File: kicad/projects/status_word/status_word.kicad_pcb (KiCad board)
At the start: 2 copper layers, 203.2 x 97.8 mm, 9 parts, among them J1 peripheral_addr_bus_connector, J2 peripheral_aux_connector, J3 peripheral_membank_connector

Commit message: WIP on status word
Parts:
- added C2: C, Capacitor_THT:C_Disc_D5.0mm_W2.5mm_P5.00mm, F.Cu at (-15.6, 66.9)
- added C3: C, Capacitor_THT:C_Disc_D5.0mm_W2.5mm_P5.00mm, F.Cu at (-15.6, 71.0)
- added C4: C, Capacitor_THT:C_Disc_D5.0mm_W2.5mm_P5.00mm, F.Cu at (-15.6, 75.0)
- added C5: C, Capacitor_THT:C_Disc_D5.0mm_W2.5mm_P5.00mm, F.Cu at (-15.6, 79.1)
- added C6: C, Capacitor_THT:C_Disc_D5.0mm_W2.5mm_P5.00mm, F.Cu at (-15.6, 83.1)
- added C7: C, Capacitor_THT:C_Disc_D5.0mm_W2.5mm_P5.00mm, F.Cu at (-15.6, 87.2)
- added D1: LED, sixteen-bit-computer:LED_D5.0mm_Horizontal_O3.81mm_Z3.0mm, F.Cu at (251.5, 63.5)
- added D10: LED, sixteen-bit-computer:LED_D5.0mm_Horizontal_O3.81mm_Z3.0mm, F.Cu at (194.3, 63.5)
- added D11: LED, sixteen-bit-computer:LED_D5.0mm_Horizontal_O3.81mm_Z3.0mm, F.Cu at (188.0, 63.5)
- added D12: LED, sixteen-bit-computer:LED_D5.0mm_Horizontal_O3.81mm_Z3.0mm, F.Cu at (181.6, 63.5)
- added D13: LED, sixteen-bit-computer:LED_D5.0mm_Horizontal_O3.81mm_Z3.0mm, F.Cu at (175.3, 63.5)
- added D14: LED, sixteen-bit-computer:LED_D5.0mm_Horizontal_O3.81mm_Z3.0mm, F.Cu at (168.9, 63.5)
- added D15: LED, sixteen-bit-computer:LED_D5.0mm_Horizontal_O3.81mm_Z3.0mm, F.Cu at (162.6, 63.5)
- added D16: LED, sixteen-bit-computer:LED_D5.0mm_Horizontal_O3.81mm_Z3.0mm, F.Cu at (156.2, 63.5)
- added D2: LED, sixteen-bit-computer:LED_D5.0mm_Horizontal_O3.81mm_Z3.0mm, F.Cu at (245.1, 63.5)
- added D3: LED, sixteen-bit-computer:LED_D5.0mm_Horizontal_O3.81mm_Z3.0mm, F.Cu at (238.8, 63.5)
- added D4: LED, sixteen-bit-computer:LED_D5.0mm_Horizontal_O3.81mm_Z3.0mm, F.Cu at (232.4, 63.5)
- added D5: LED, sixteen-bit-computer:LED_D5.0mm_Horizontal_O3.81mm_Z3.0mm, F.Cu at (226.1, 63.5)
- added D6: LED, sixteen-bit-computer:LED_D5.0mm_Horizontal_O3.81mm_Z3.0mm, F.Cu at (219.7, 63.5)
- added D7: LED, sixteen-bit-computer:LED_D5.0mm_Horizontal_O3.81mm_Z3.0mm, F.Cu at (213.4, 63.5)
- added D8: LED, sixteen-bit-computer:LED_D5.0mm_Horizontal_O3.81mm_Z3.0mm, F.Cu at (207.0, 63.5)
- added D9: LED, sixteen-bit-computer:LED_D5.0mm_Horizontal_O3.81mm_Z3.0mm, F.Cu at (200.7, 63.5)
- added J10: Conn_01x02_Pin, Connector_PinHeader_2.54mm:PinHeader_1x02_P2.54mm_Vertical, F.Cu at (137.2, 53.3)
- added J11: Conn_01x02_Pin, Connector_PinHeader_2.54mm:PinHeader_1x02_P2.54mm_Vertical, F.Cu at (124.5, 53.3)
- added J12: Conn_01x02_Pin, Connector_PinHeader_2.54mm:PinHeader_1x02_P2.54mm_Vertical, F.Cu at (114.3, 53.3)
- added J13: Conn_01x02_Pin, Connector_PinHeader_2.54mm:PinHeader_1x02_P2.54mm_Vertical, F.Cu at (104.1, 53.3)
- added J14: Conn_01x08_Socket, Connector_PinSocket_2.54mm:PinSocket_1x08_P2.54mm_Horizontal, F.Cu at (61.0, 81.3)
- added J4: Conn_01x16_Socket, Connector_PinSocket_2.54mm:PinSocket_1x16_P2.54mm_Horizontal, F.Cu at (91.4, 61.0)
- added J5: Conn_01x04_Socket, Connector_PinSocket_2.54mm:PinSocket_1x04_P2.54mm_Horizontal, F.Cu at (61.0, 116.8)
- added J6: Conn_01x02_Pin, Connector_PinHeader_2.54mm:PinHeader_1x02_P2.54mm_Vertical, F.Cu at (109.2, 63.5)
- added J7: Conn_01x02_Pin, Connector_PinHeader_2.54mm:PinHeader_1x02_P2.54mm_Vertical, F.Cu at (119.4, 63.5)
- added J8: Conn_01x02_Pin, Connector_PinHeader_2.54mm:PinHeader_1x02_P2.54mm_Vertical, F.Cu at (132.1, 63.5)
- added J9: Conn_01x02_Pin, Connector_PinHeader_2.54mm:PinHeader_1x02_P2.54mm_Vertical, F.Cu at (144.8, 63.5)
- added RN1: R_Network08_US, Resistor_THT:R_Array_SIP9, F.Cu at (221.0, 71.1)
- added RN2: R_Network08_US, Resistor_THT:R_Array_SIP9, F.Cu at (170.2, 71.1)
- added RN3: R_Network08_US, Resistor_THT:R_Array_SIP9, F.Cu at (66.0, 101.6)
- added U1: 74HC10, Package_DIP:DIP-14_W7.62mm_Socket, F.Cu at (127.0, 132.1)
- added U2: 74HC377, Package_DIP:DIP-20_W7.62mm_Socket, F.Cu at (221.0, 132.1)
- added U3: 74HC377, Package_DIP:DIP-20_W7.62mm_Socket, F.Cu at (185.4, 132.1)
- added U4: 74HC245, Package_DIP:DIP-20_W7.62mm_Socket, F.Cu at (221.0, 114.3)
- added U5: 74HC245, Package_DIP:DIP-20_W7.62mm_Socket, F.Cu at (185.4, 114.3)
- added U6: 74HC245, Package_DIP:DIP-20_W7.62mm_Socket, F.Cu at (218.4, 86.4)
- added U7: 74HC245, Package_DIP:DIP-20_W7.62mm_Socket, F.Cu at (167.6, 86.4)
- moved C98 32.4 mm to (266.7, 83.8)
- moved C99 28.4 mm to (86.4, 124.5)
- moved C97 18.3 mm to (73.7, 71.1)
- turned J2 to 0 degrees
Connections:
- net /RFM renamed /MEM_ACT
- net /WTM renamed /~{RFM}/WTM

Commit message: Status word schematic complete - WIP on PCB.
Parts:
- removed TP1: TestPoint, Connector_Pin:Pin_D1.0mm_L10.0mm
- added J15: Conn_01x03_Pin, Connector_PinHeader_2.54mm:PinHeader_1x03_P2.54mm_Horizontal, F.Cu at (63.5, 111.8)
- added R1: 10K, Resistor_THT:R_Axial_DIN0207_L6.3mm_D2.5mm_P10.16mm_Horizontal, F.Cu at (27.9, 94.5)
- added R2: 10K, Resistor_THT:R_Axial_DIN0207_L6.3mm_D2.5mm_P10.16mm_Horizontal, F.Cu at (27.9, 98.6)
- added R3: 10K, Resistor_THT:R_Axial_DIN0207_L6.3mm_D2.5mm_P10.16mm_Horizontal, F.Cu at (27.9, 102.6)
- added R4: 10K, Resistor_THT:R_Axial_DIN0207_L6.3mm_D2.5mm_P10.16mm_Horizontal, F.Cu at (27.9, 106.7)
- RN1, RN2: value R_Network08_US -> 2K
- moved C3 235.1 mm to (213.4, 124.4), turned to 90 degrees
- moved C7 223.9 mm to (208.3, 86.3), turned to 90 degrees
- moved C4 202.0 mm to (180.3, 124.4), turned to 90 degrees
- moved C6 173.1 mm to (157.5, 86.3), turned to 90 degrees
- moved C2 172.7 mm to (147.3, 124.4), turned to 90 degrees
- moved C5 137.5 mm to (114.3, 124.4), turned to 90 degrees
- moved RN2 71.1 mm to (241.3, 72.4), turned to 180 degrees
- moved U2 68.8 mm to (152.4, 127.0)
- moved U5 67.3 mm to (119.4, 127.0)
- moved U6 55.9 mm to (162.6, 88.9)
- moved C97 51.1 mm to (22.6, 71.6)
- moved U1 48.3 mm to (124.5, 83.8)
- moved U7 45.8 mm to (213.4, 88.9)
- moved C1 38.8 mm to (119.4, 76.2), turned to -90 degrees
- moved U4 37.8 mm to (185.4, 127.0)
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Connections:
- C1 pad 1: unconnected-(C1-Pad1) -> VCC
- C1 pad 2: unconnected-(C1-Pad2) -> GND
- C2 pad 1: unconnected-(C2-Pad1) -> GND
- C2 pad 2: unconnected-(C2-Pad2) -> VCC
- C3 pad 1: unconnected-(C3-Pad1) -> GND
- C3 pad 2: unconnected-(C3-Pad2) -> VCC
- C4 pad 1: unconnected-(C4-Pad1) -> GND
- C4 pad 2: unconnected-(C4-Pad2) -> VCC
- C5 pad 1: unconnected-(C5-Pad1) -> GND
- C5 pad 2: unconnected-(C5-Pad2) -> VCC
- C6 pad 1: unconnected-(C6-Pad1) -> GND
- C6 pad 2: unconnected-(C6-Pad2) -> VCC
- C7 pad 1: unconnected-(C7-Pad1) -> GND
- C7 pad 2: unconnected-(C7-Pad2) -> VCC
- D1 pad 1: unconnected-(D1-K-Pad1) -> Net-(D1-K)
- D1 pad 2: unconnected-(D1-A-Pad2) -> Net-(D1-A)
- D10 pad 1: unconnected-(D10-K-Pad1) -> Net-(D10-K)
- D10 pad 2: unconnected-(D10-A-Pad2) -> Net-(D10-A)
- D11 pad 1: unconnected-(D11-K-Pad1) -> Net-(D11-K)
- D11 pad 2: unconnected-(D11-A-Pad2) -> Net-(D11-A)
- D12 pad 1: unconnected-(D12-K-Pad1) -> Net-(D12-K)
- D12 pad 2: unconnected-(D12-A-Pad2) -> Net-(D12-A)
- D13 pad 1: unconnected-(D13-K-Pad1) -> Net-(D13-K)
- D13 pad 2: unconnected-(D13-A-Pad2) -> Net-(D13-A)
- D14 pad 1: unconnected-(D14-K-Pad1) -> Net-(D14-K)
- D14 pad 2: unconnected-(D14-A-Pad2) -> Net-(D14-A)
- D15 pad 1: unconnected-(D15-K-Pad1) -> Net-(D15-K)
- D15 pad 2: unconnected-(D15-A-Pad2) -> Net-(D15-A)
- D16 pad 1: unconnected-(D16-K-Pad1) -> Net-(D16-K)
- D16 pad 2: unconnected-(D16-A-Pad2) -> Net-(D16-A)
- D2 pad 1: unconnected-(D2-K-Pad1) -> Net-(D2-K)
- D2 pad 2: unconnected-(D2-A-Pad2) -> Net-(D2-A)
- D3 pad 1: unconnected-(D3-K-Pad1) -> Net-(D3-K)
- D3 pad 2: unconnected-(D3-A-Pad2) -> Net-(D3-A)
- D4 pad 1: unconnected-(D4-K-Pad1) -> Net-(D4-K)
- D4 pad 2: unconnected-(D4-A-Pad2) -> Net-(D4-A)
- D5 pad 1: unconnected-(D5-K-Pad1) -> Net-(D5-K)
- D5 pad 2: unconnected-(D5-A-Pad2) -> Net-(D5-A)
- D6 pad 1: unconnected-(D6-K-Pad1) -> Net-(D6-K)
- D6 pad 2: unconnected-(D6-A-Pad2) -> Net-(D6-A)
- D7 pad 1: unconnected-(D7-K-Pad1) -> Net-(D7-K)
- D7 pad 2: unconnected-(D7-A-Pad2) -> Net-(D7-A)
- D8 pad 1: unconnected-(D8-K-Pad1) -> Net-(D8-K)
- D8 pad 2: unconnected-(D8-A-Pad2) -> Net-(D8-A)
- D9 pad 1: unconnected-(D9-K-Pad1) -> Net-(D9-K)
- D9 pad 2: unconnected-(D9-A-Pad2) -> Net-(D9-A)
- J1 pad 17: /ADDR_BUS_00 -> unconnected-(J1-A_00-Pad17)
- J1 pad 18: /ADDR_BUS_01 -> unconnected-(J1-A_01-Pad18)
- J1 pad 19: /ADDR_BUS_02 -> unconnected-(J1-A_02-Pad19)
- J1 pad 20: /ADDR_BUS_03 -> unconnected-(J1-A_03-Pad20)
- J1 pad 21: /ADDR_BUS_04 -> unconnected-(J1-A_04-Pad21)
- J1 pad 22: /ADDR_BUS_05 -> unconnected-(J1-A_05-Pad22)
- J1 pad 23: /ADDR_BUS_06 -> unconnected-(J1-A_06-Pad23)
- J1 pad 24: /ADDR_BUS_07 -> unconnected-(J1-A_07-Pad24)
- J1 pad 25: /ADDR_BUS_08 -> unconnected-(J1-A_08-Pad25)
- J1 pad 26: /ADDR_BUS_09 -> unconnected-(J1-A_09-Pad26)
- J1 pad 27: /ADDR_BUS_10 -> unconnected-(J1-A_10-Pad27)
- J1 pad 28: /ADDR_BUS_11 -> unconnected-(J1-A_11-Pad28)
- J1 pad 29: /ADDR_BUS_12 -> unconnected-(J1-A_12-Pad29)
- J1 pad 30: /ADDR_BUS_13 -> unconnected-(J1-A_13-Pad30)
- J1 pad 31: /ADDR_BUS_14 -> unconnected-(J1-A_14-Pad31)
- J1 pad 32: /ADDR_BUS_15 -> unconnected-(J1-A_15-Pad32)
- J10 pad 1: unconnected-(J10-Pin_1-Pad1) -> GND
- J10 pad 2: unconnected-(J10-Pin_2-Pad2) -> GND
- J11 pad 1: unconnected-(J11-Pin_1-Pad1) -> /CONTENT_14
- J11 pad 2: unconnected-(J11-Pin_2-Pad2) -> /CONTENT_14
- J12 pad 1: unconnected-(J12-Pin_1-Pad1) -> GND
- J12 pad 2: unconnected-(J12-Pin_2-Pad2) -> GND
- J13 pad 1: unconnected-(J13-Pin_1-Pad1) -> /CONTENT_15
- J13 pad 2: unconnected-(J13-Pin_2-Pad2) -> /CONTENT_15
- J14 pad 1: unconnected-(J14-Pin_1-Pad1) -> /EXT_7
- J14 pad 2: unconnected-(J14-Pin_2-Pad2) -> /EXT_6
- J14 pad 3: unconnected-(J14-Pin_3-Pad3) -> /EXT_5
- J14 pad 4: unconnected-(J14-Pin_4-Pad4) -> /EXT_4
- J14 pad 5: unconnected-(J14-Pin_5-Pad5) -> /EXT_3
- J14 pad 6: unconnected-(J14-Pin_6-Pad6) -> /EXT_2
- J14 pad 7: unconnected-(J14-Pin_7-Pad7) -> /EXT_1
- J14 pad 8: unconnected-(J14-Pin_8-Pad8) -> /EXT_0
- J2 pad 14: /RESET -> unconnected-(J2-RST-Pad14)
- J2 pad 8: /CTL_CLK -> unconnected-(J2-CCLK-Pad8)
- J3 pad 1: /BANK_BUS_00 -> unconnected-(J3-B_00-Pad1)
- J3 pad 10: /BANK_BUS_09 -> unconnected-(J3-B_09-Pad10)
- J3 pad 11: /BANK_BUS_10 -> unconnected-(J3-B_10-Pad11)
- J3 pad 12: /BANK_BUS_11 -> unconnected-(J3-B_11-Pad12)
- J3 pad 13: /BANK_BUS_12 -> unconnected-(J3-B_12-Pad13)
- J3 pad 14: /BANK_BUS_13 -> unconnected-(J3-B_13-Pad14)
- J3 pad 15: /BANK_BUS_14 -> unconnected-(J3-B_14-Pad15)
- J3 pad 16: /BANK_BUS_15 -> unconnected-(J3-B_15-Pad16)
- J3 pad 2: /BANK_BUS_01 -> unconnected-(J3-B_01-Pad2)
- J3 pad 3: /BANK_BUS_02 -> unconnected-(J3-B_02-Pad3)
- J3 pad 4: /BANK_BUS_03 -> unconnected-(J3-B_03-Pad4)
- J3 pad 5: /BANK_BUS_04 -> unconnected-(J3-B_04-Pad5)
- J3 pad 6: /BANK_BUS_05 -> unconnected-(J3-B_05-Pad6)
- J3 pad 7: /BANK_BUS_06 -> unconnected-(J3-B_06-Pad7)
- J3 pad 8: /BANK_BUS_07 -> unconnected-(J3-B_07-Pad8)
- J3 pad 9: /BANK_BUS_08 -> unconnected-(J3-B_08-Pad9)
- J4 pad 1: unconnected-(J4-Pin_1-Pad1) -> /CONTENT_00
- J4 pad 10: unconnected-(J4-Pin_10-Pad10) -> /CONTENT_09
- J4 pad 11: unconnected-(J4-Pin_11-Pad11) -> /CONTENT_10
- J4 pad 12: unconnected-(J4-Pin_12-Pad12) -> /CONTENT_11
- J4 pad 13: unconnected-(J4-Pin_13-Pad13) -> /CONTENT_12
- J4 pad 14: unconnected-(J4-Pin_14-Pad14) -> /CONTENT_13
- J4 pad 15: unconnected-(J4-Pin_15-Pad15) -> /CONTENT_14
- J4 pad 16: unconnected-(J4-Pin_16-Pad16) -> /CONTENT_15
- J4 pad 2: unconnected-(J4-Pin_2-Pad2) -> /CONTENT_01
- J4 pad 3: unconnected-(J4-Pin_3-Pad3) -> /CONTENT_02
- J4 pad 4: unconnected-(J4-Pin_4-Pad4) -> /CONTENT_03
- J4 pad 5: unconnected-(J4-Pin_5-Pad5) -> /CONTENT_04
- J4 pad 6: unconnected-(J4-Pin_6-Pad6) -> /CONTENT_05
- J4 pad 7: unconnected-(J4-Pin_7-Pad7) -> /CONTENT_06
- J4 pad 8: unconnected-(J4-Pin_8-Pad8) -> /CONTENT_07
- J4 pad 9: unconnected-(J4-Pin_9-Pad9) -> /CONTENT_08
- J5 pad 1: unconnected-(J5-Pin_1-Pad1) -> /ADDRESSED
- J5 pad 2: unconnected-(J5-Pin_2-Pad2) -> /ADDRESSED
- J5 pad 3: unconnected-(J5-Pin_3-Pad3) -> /ADDRESSED
- J5 pad 4: unconnected-(J5-Pin_4-Pad4) -> /ADDRESSED
- J6 pad 1: unconnected-(J6-Pin_1-Pad1) -> GND
- J6 pad 2: unconnected-(J6-Pin_2-Pad2) -> GND
- J7 pad 1: unconnected-(J7-Pin_1-Pad1) -> /CONTENT_12
- J7 pad 2: unconnected-(J7-Pin_2-Pad2) -> /CONTENT_12
- J8 pad 1: unconnected-(J8-Pin_1-Pad1) -> GND
- J8 pad 2: unconnected-(J8-Pin_2-Pad2) -> GND
- J9 pad 1: unconnected-(J9-Pin_1-Pad1) -> /CONTENT_13
- J9 pad 2: unconnected-(J9-Pin_2-Pad2) -> /CONTENT_13
- RN1 pad 1: unconnected-(RN1-common-Pad1) -> GND
- RN1 pad 2: unconnected-(RN1-R1-Pad2) -> Net-(D9-K)
- RN1 pad 3: unconnected-(RN1-R2-Pad3) -> Net-(D10-K)
- RN1 pad 4: unconnected-(RN1-R3-Pad4) -> Net-(D11-K)
- RN1 pad 5: unconnected-(RN1-R4-Pad5) -> Net-(D12-K)
- RN1 pad 6: unconnected-(RN1-R5-Pad6) -> Net-(D13-K)
- RN1 pad 7: unconnected-(RN1-R6-Pad7) -> Net-(D14-K)
- RN1 pad 8: unconnected-(RN1-R7-Pad8) -> Net-(D15-K)
- RN1 pad 9: unconnected-(RN1-R8-Pad9) -> Net-(D16-K)
- RN2 pad 1: unconnected-(RN2-common-Pad1) -> GND
- RN2 pad 2: unconnected-(RN2-R1-Pad2) -> Net-(D1-K)
- RN2 pad 3: unconnected-(RN2-R2-Pad3) -> Net-(D2-K)
- RN2 pad 4: unconnected-(RN2-R3-Pad4) -> Net-(D3-K)
- RN2 pad 5: unconnected-(RN2-R4-Pad5) -> Net-(D4-K)
- RN2 pad 6: unconnected-(RN2-R5-Pad6) -> Net-(D5-K)
- RN2 pad 7: unconnected-(RN2-R6-Pad7) -> Net-(D6-K)
- RN2 pad 8: unconnected-(RN2-R7-Pad8) -> Net-(D7-K)
- RN2 pad 9: unconnected-(RN2-R8-Pad9) -> Net-(D8-K)
- RN3 pad 1: unconnected-(RN3-common-Pad1) -> GND
- RN3 pad 2: unconnected-(RN3-R1-Pad2) -> /EXT_0
- RN3 pad 3: unconnected-(RN3-R2-Pad3) -> /EXT_1
- RN3 pad 4: unconnected-(RN3-R3-Pad4) -> /EXT_2
- RN3 pad 5: unconnected-(RN3-R4-Pad5) -> /EXT_3
- RN3 pad 6: unconnected-(RN3-R5-Pad6) -> /EXT_4
- RN3 pad 7: unconnected-(RN3-R6-Pad7) -> /EXT_5
- RN3 pad 8: unconnected-(RN3-R7-Pad8) -> /EXT_6
- RN3 pad 9: unconnected-(RN3-R8-Pad9) -> /EXT_7
- U1 pad 1: unconnected-(U1-Pad1) -> /MEM_ACT
- U1 pad 10: unconnected-(U1-Pad10) -> /~{RFM}/WTM
- U1 pad 11: unconnected-(U1-Pad11) -> /~{RFM}/WTM
- U1 pad 12: unconnected-(U1-Pad12) -> /~{WTM}
- U1 pad 13: unconnected-(U1-Pad13) -> /~{RFM}/WTM
- U1 pad 14: unconnected-(U1D-VCC-Pad14) -> VCC
- U1 pad 2: unconnected-(U1-Pad2) -> /ADDRESSED
- U1 pad 3: unconnected-(U1-Pad3) -> /MEM_ACT
- U1 pad 4: unconnected-(U1-Pad4) -> /ADDRESSED
- U1 pad 5: unconnected-(U1-Pad5) -> /RFM/~{WTM}
- U1 pad 6: unconnected-(U1-Pad6) -> /~{RFM}
- U1 pad 7: unconnected-(U1D-GND-Pad7) -> GND
- U1 pad 8: unconnected-(U1-Pad8) -> /RFM/~{WTM}
- U1 pad 9: unconnected-(U1-Pad9) -> /~{RFM}/WTM
- U2 pad 1: unconnected-(U2-~{E}-Pad1) -> /~{WTM}
- U2 pad 10: unconnected-(U2-GND-Pad10) -> GND
- U2 pad 11: unconnected-(U2-CP-Pad11) -> /DATA_CLK
- U2 pad 12: unconnected-(U2-Q4-Pad12) -> /CONTENT_12
- U2 pad 13: unconnected-(U2-D4-Pad13) -> /DATA_BUS_12
- U2 pad 14: unconnected-(U2-D5-Pad14) -> /DATA_BUS_13
- U2 pad 15: unconnected-(U2-Q5-Pad15) -> /CONTENT_13
- U2 pad 16: unconnected-(U2-Q6-Pad16) -> /CONTENT_14
- U2 pad 17: unconnected-(U2-D6-Pad17) -> /DATA_BUS_14
- U2 pad 18: unconnected-(U2-D7-Pad18) -> /DATA_BUS_15
- U2 pad 19: unconnected-(U2-Q7-Pad19) -> /CONTENT_15
- U2 pad 2: unconnected-(U2-Q0-Pad2) -> /CONTENT_08
- U2 pad 20: unconnected-(U2-VCC-Pad20) -> VCC
- U2 pad 3: unconnected-(U2-D0-Pad3) -> /DATA_BUS_08
- U2 pad 4: unconnected-(U2-D1-Pad4) -> /DATA_BUS_09
- U2 pad 5: unconnected-(U2-Q1-Pad5) -> /CONTENT_09
- U2 pad 6: unconnected-(U2-Q2-Pad6) -> /CONTENT_10
- U2 pad 7: unconnected-(U2-D2-Pad7) -> /DATA_BUS_10
- U2 pad 8: unconnected-(U2-D3-Pad8) -> /DATA_BUS_11
- U2 pad 9: unconnected-(U2-Q3-Pad9) -> /CONTENT_11
- U3 pad 1: unconnected-(U3-~{E}-Pad1) -> /~{WTM}
- U3 pad 10: unconnected-(U3-GND-Pad10) -> GND
- U3 pad 11: unconnected-(U3-CP-Pad11) -> /DATA_CLK
- U3 pad 12: unconnected-(U3-Q4-Pad12) -> /CONTENT_04
- U3 pad 13: unconnected-(U3-D4-Pad13) -> /DATA_BUS_04
- U3 pad 14: unconnected-(U3-D5-Pad14) -> /DATA_BUS_05
- U3 pad 15: unconnected-(U3-Q5-Pad15) -> /CONTENT_05
- U3 pad 16: unconnected-(U3-Q6-Pad16) -> /CONTENT_06
- U3 pad 17: unconnected-(U3-D6-Pad17) -> /DATA_BUS_06
- U3 pad 18: unconnected-(U3-D7-Pad18) -> /DATA_BUS_07
- U3 pad 19: unconnected-(U3-Q7-Pad19) -> /CONTENT_07
- U3 pad 2: unconnected-(U3-Q0-Pad2) -> /CONTENT_00
- U3 pad 20: unconnected-(U3-VCC-Pad20) -> VCC
- U3 pad 3: unconnected-(U3-D0-Pad3) -> /DATA_BUS_00
- U3 pad 4: unconnected-(U3-D1-Pad4) -> /DATA_BUS_01
- U3 pad 5: unconnected-(U3-Q1-Pad5) -> /CONTENT_01
- U3 pad 6: unconnected-(U3-Q2-Pad6) -> /CONTENT_02
- U3 pad 7: unconnected-(U3-D2-Pad7) -> /DATA_BUS_02
- U3 pad 8: unconnected-(U3-D3-Pad8) -> /DATA_BUS_03
- U3 pad 9: unconnected-(U3-Q3-Pad9) -> /CONTENT_03
- U4 pad 10: unconnected-(U4-GND-Pad10) -> GND
- U4 pad 11: unconnected-(U4-B8-Pad11) -> /CONTENT_04
- U4 pad 12: unconnected-(U4-B7-Pad12) -> /CONTENT_03
- U4 pad 13: unconnected-(U4-B6-Pad13) -> /CONTENT_05
- U4 pad 14: unconnected-(U4-B5-Pad14) -> /CONTENT_02
- U4 pad 15: unconnected-(U4-B4-Pad15) -> /CONTENT_06
- U4 pad 16: unconnected-(U4-B3-Pad16) -> /CONTENT_01
- U4 pad 17: unconnected-(U4-B2-Pad17) -> /CONTENT_07
- U4 pad 18: unconnected-(U4-B1-Pad18) -> /CONTENT_00
- U4 pad 19: unconnected-(U4-~{OE}-Pad19) -> /~{RFM}
- U4 pad 2: unconnected-(U4-A1-Pad2) -> /DATA_BUS_00
- U4 pad 20: unconnected-(U4-VCC-Pad20) -> VCC
- U4 pad 3: unconnected-(U4-A2-Pad3) -> /DATA_BUS_07
- U4 pad 4: unconnected-(U4-A3-Pad4) -> /DATA_BUS_01
- U4 pad 5: unconnected-(U4-A4-Pad5) -> /DATA_BUS_06
- U4 pad 6: unconnected-(U4-A5-Pad6) -> /DATA_BUS_02
- U4 pad 7: unconnected-(U4-A6-Pad7) -> /DATA_BUS_05
- U4 pad 8: unconnected-(U4-A7-Pad8) -> /DATA_BUS_03
- U4 pad 9: unconnected-(U4-A8-Pad9) -> /DATA_BUS_04
- U5 pad 10: unconnected-(U5-GND-Pad10) -> GND
- U5 pad 11: unconnected-(U5-B8-Pad11) -> /EXT_0
- U5 pad 12: unconnected-(U5-B7-Pad12) -> /EXT_1
- U5 pad 13: unconnected-(U5-B6-Pad13) -> /EXT_2
- U5 pad 14: unconnected-(U5-B5-Pad14) -> /EXT_3
- U5 pad 15: unconnected-(U5-B4-Pad15) -> /EXT_4
- U5 pad 16: unconnected-(U5-B3-Pad16) -> /EXT_5
- U5 pad 17: unconnected-(U5-B2-Pad17) -> /EXT_6
- U5 pad 18: unconnected-(U5-B1-Pad18) -> /EXT_7
- U5 pad 19: unconnected-(U5-~{OE}-Pad19) -> /~{RFM}
- U5 pad 2: unconnected-(U5-A1-Pad2) -> /DATA_BUS_08
- U5 pad 20: unconnected-(U5-VCC-Pad20) -> VCC
- U5 pad 3: unconnected-(U5-A2-Pad3) -> /DATA_BUS_09
- U5 pad 4: unconnected-(U5-A3-Pad4) -> /DATA_BUS_10
- U5 pad 5: unconnected-(U5-A4-Pad5) -> /DATA_BUS_11
- U5 pad 6: unconnected-(U5-A5-Pad6) -> /DATA_BUS_12
- U5 pad 7: unconnected-(U5-A6-Pad7) -> /DATA_BUS_13
- U5 pad 8: unconnected-(U5-A7-Pad8) -> /DATA_BUS_14
- U5 pad 9: unconnected-(U5-A8-Pad9) -> /DATA_BUS_15
- U6 pad 1: unconnected-(U6-DIR-Pad1) -> VCC
- U6 pad 10: unconnected-(U6-GND-Pad10) -> GND
- U6 pad 11: unconnected-(U6-B8-Pad11) -> Net-(D9-A)
- U6 pad 12: unconnected-(U6-B7-Pad12) -> Net-(D10-A)
- U6 pad 13: unconnected-(U6-B6-Pad13) -> Net-(D11-A)
- U6 pad 14: unconnected-(U6-B5-Pad14) -> Net-(D12-A)
- U6 pad 15: unconnected-(U6-B4-Pad15) -> Net-(D13-A)
- U6 pad 16: unconnected-(U6-B3-Pad16) -> Net-(D14-A)
- U6 pad 17: unconnected-(U6-B2-Pad17) -> Net-(D15-A)
- U6 pad 18: unconnected-(U6-B1-Pad18) -> Net-(D16-A)
- U6 pad 19: unconnected-(U6-~{OE}-Pad19) -> /LED_~{OE}
- U6 pad 2: unconnected-(U6-A1-Pad2) -> /CONTENT_15
- U6 pad 20: unconnected-(U6-VCC-Pad20) -> VCC
- U6 pad 3: unconnected-(U6-A2-Pad3) -> /CONTENT_14
- U6 pad 4: unconnected-(U6-A3-Pad4) -> /CONTENT_13
- U6 pad 5: unconnected-(U6-A4-Pad5) -> /CONTENT_12
- U6 pad 6: unconnected-(U6-A5-Pad6) -> /CONTENT_11
- U6 pad 7: unconnected-(U6-A6-Pad7) -> /CONTENT_10
- U6 pad 8: unconnected-(U6-A7-Pad8) -> /CONTENT_09
- U6 pad 9: unconnected-(U6-A8-Pad9) -> /CONTENT_08
- U7 pad 1: unconnected-(U7-DIR-Pad1) -> VCC
- U7 pad 10: unconnected-(U7-GND-Pad10) -> GND
- U7 pad 11: unconnected-(U7-B8-Pad11) -> Net-(D1-A)
- U7 pad 12: unconnected-(U7-B7-Pad12) -> Net-(D2-A)
- U7 pad 13: unconnected-(U7-B6-Pad13) -> Net-(D3-A)
- U7 pad 14: unconnected-(U7-B5-Pad14) -> Net-(D4-A)
- U7 pad 15: unconnected-(U7-B4-Pad15) -> Net-(D5-A)
- U7 pad 16: unconnected-(U7-B3-Pad16) -> Net-(D6-A)
- U7 pad 17: unconnected-(U7-B2-Pad17) -> Net-(D7-A)
- U7 pad 18: unconnected-(U7-B1-Pad18) -> Net-(D8-A)
- U7 pad 19: unconnected-(U7-~{OE}-Pad19) -> /LED_~{OE}
- U7 pad 2: unconnected-(U7-A1-Pad2) -> /CONTENT_07
- U7 pad 20: unconnected-(U7-VCC-Pad20) -> VCC
- U7 pad 3: unconnected-(U7-A2-Pad3) -> /CONTENT_06
- U7 pad 4: unconnected-(U7-A3-Pad4) -> /CONTENT_05
- U7 pad 5: unconnected-(U7-A4-Pad5) -> /CONTENT_04
- U7 pad 6: unconnected-(U7-A5-Pad6) -> /CONTENT_03
- U7 pad 7: unconnected-(U7-A6-Pad7) -> /CONTENT_02
- U7 pad 8: unconnected-(U7-A7-Pad8) -> /CONTENT_01
- U7 pad 9: unconnected-(U7-A8-Pad9) -> /CONTENT_00
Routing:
- net /CONTENT_03: track 0.00 -> 44.2 mm
- net /CONTENT_01: track 0.00 -> 44.2 mm
- net /CONTENT_02: track 0.00 -> 44.2 mm
- net /CONTENT_00: track 0.00 -> 44.2 mm
- net /CONTENT_08: track 0.00 -> 41.4 mm
- net /CONTENT_11: track 0.00 -> 41.2 mm
- net /CONTENT_09: track 0.00 -> 41.2 mm
- net /CONTENT_10: track 0.00 -> 41.2 mm
- net /CONTENT_07: track 0.00 -> 36.6 mm
- net /CONTENT_05: track 0.00 -> 36.6 mm
- net /CONTENT_06: track 0.00 -> 35.6 mm
- net /CONTENT_04: track 0.00 -> 34.8 mm
- net /CONTENT_15: track 0.00 -> 33.0 mm
- net /CONTENT_14: track 0.00 -> 33.0 mm
- net /CONTENT_13: track 0.00 -> 33.0 mm
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
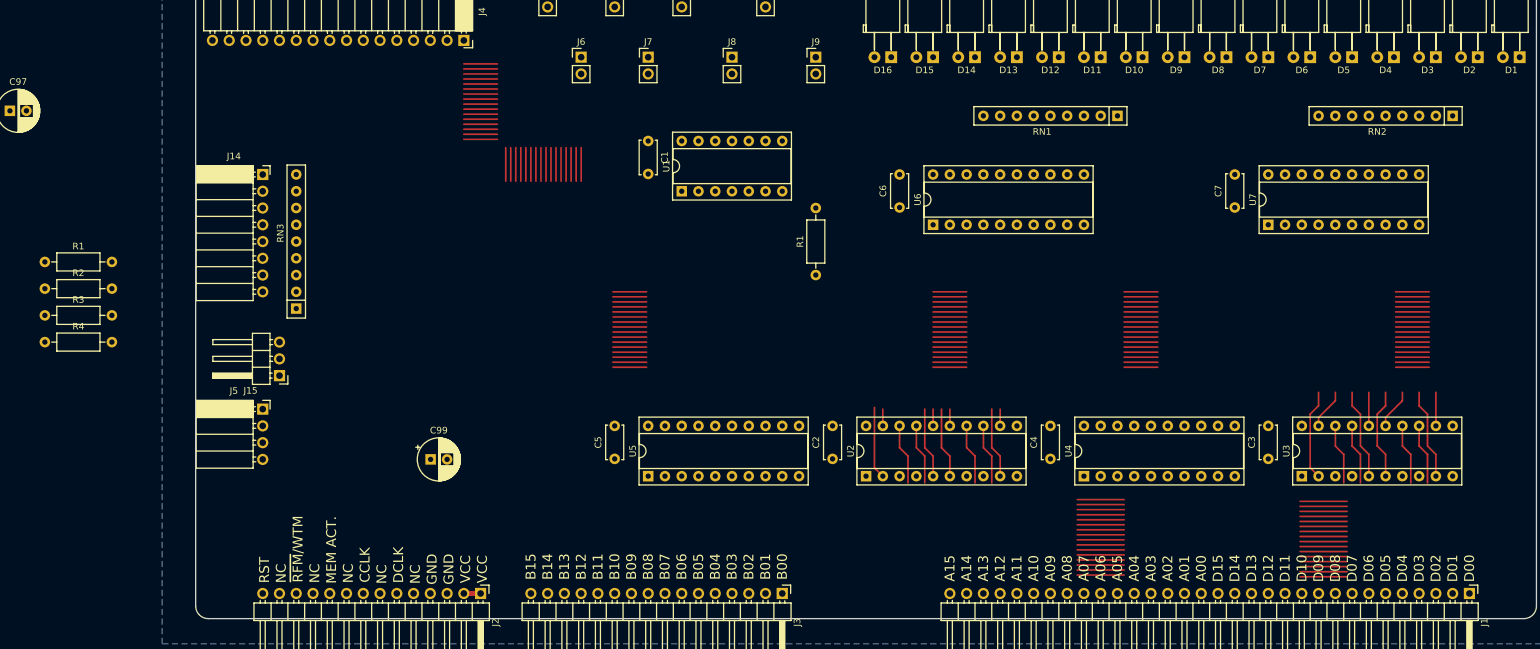
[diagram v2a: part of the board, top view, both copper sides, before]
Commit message: WIP on status word PCB
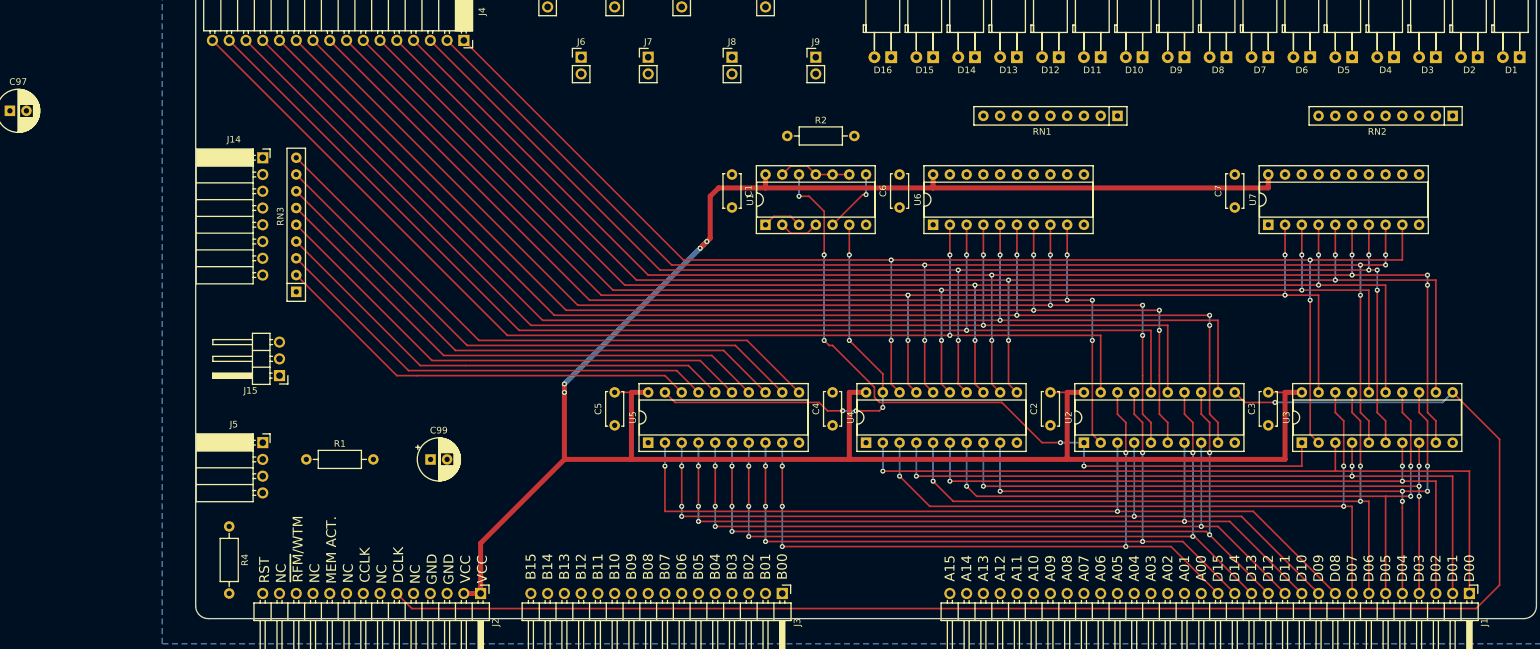
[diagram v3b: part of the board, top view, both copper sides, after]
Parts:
- removed the R1 at (144.8, 96.5)
- removed R3: 10K, Resistor_THT:R_Axial_DIN0207_L6.3mm_D2.5mm_P10.16mm_Horizontal
- moved R2 114.9 mm to (140.5, 75.4)
- moved R1 49.7 mm to (67.6, 124.5)
- moved R4 39.5 mm to (55.9, 134.6), turned to -90 degrees
- moved C2 33.4 mm to (180.3, 119.3)
- moved C4 33.4 mm to (147.3, 119.3)
- moved U2 33.4 mm to (185.4, 121.9)
- moved U4 33.4 mm to (152.4, 121.9)
- moved C1 13.7 mm to (132.1, 81.3)
- moved U1 13.7 mm to (137.2, 88.9)
- moved C3 5.08 mm to (213.4, 119.3)
- moved C5 5.08 mm to (114.3, 119.3)
- moved J5 5.08 mm to (61.0, 121.9)
- moved U3 5.08 mm to (218.4, 121.9)
- moved U5 5.08 mm to (119.4, 121.9)
- moved J14 2.54 mm to (61.0, 78.7)
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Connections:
- U5 pad 11: /EXT_0 -> /EXT_7
- U5 pad 12: /EXT_1 -> /EXT_6
- U5 pad 13: /EXT_2 -> /EXT_5
- U5 pad 14: /EXT_3 -> /EXT_4
- U5 pad 15: /EXT_4 -> /EXT_3
- U5 pad 16: /EXT_5 -> /EXT_2
- U5 pad 17: /EXT_6 -> /EXT_1
- U5 pad 18: /EXT_7 -> /EXT_0
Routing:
- net VCC: track 2.54 -> 337.5 mm, vias 0 -> 4
- net /DATA_CLK: track 0.00 -> 236.0 mm, vias 0 -> 1
- net /CONTENT_04: track 34.8 -> 214.7 mm, vias 0 -> 4
- net /CONTENT_03: track 44.2 -> 220.3 mm, vias 0 -> 6
- net /CONTENT_06: track 35.6 -> 209.5 mm, vias 0 -> 4
- net /CONTENT_05: track 36.6 -> 209.9 mm, vias 0 -> 4
- net /CONTENT_07: track 36.6 -> 204.0 mm, vias 0 -> 4
- net /CONTENT_02: track 44.2 -> 210.5 mm, vias 0 -> 6
- net /CONTENT_00: track 44.2 -> 210.2 mm, vias 0 -> 4
- net /CONTENT_01: track 44.2 -> 209.7 mm, vias 0 -> 6
- net /CONTENT_12: track 33.0 -> 187.8 mm, vias 0 -> 2
- net /CONTENT_11: track 41.2 -> 191.8 mm, vias 0 -> 4
- net /CONTENT_14: track 33.0 -> 183.3 mm, vias 0 -> 2
- net /CONTENT_13: track 33.0 -> 183.0 mm, vias 0 -> 2
- net /CONTENT_15: track 33.0 -> 178.5 mm, vias 0 -> 2
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
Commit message: Status word PCB done - just needs tech check.
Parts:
- added J16: Conn_01x02_Pin, Connector_PinSocket_2.54mm:PinSocket_1x02_P2.54mm_Horizontal, F.Cu at (99.1, 61.0)
- added J17: Conn_01x02_Pin, Connector_PinHeader_2.54mm:PinHeader_1x02_P2.54mm_Vertical, F.Cu at (106.7, 63.5)
- RN3: value R_Network08_US -> 10K
- moved C97 196.4 mm to (215.9, 106.6), turned to 90 degrees
- moved J12 34.5 mm to (147.3, 63.5)
- moved J7 25.0 mm to (142.2, 53.3)
- moved C98 22.9 mm to (243.8, 83.8)
- moved C99 21.7 mm to (106.7, 132.1), turned to -90 degrees
- moved J9 16.3 mm to (132.1, 53.3)
- moved R1 16.1 mm to (53.3, 116.8)
- moved J10 10.2 mm to (137.2, 63.5)
- moved J13 7.62 mm to (111.8, 53.3)
- moved J6 7.62 mm to (116.8, 63.5)
- moved J8 5.08 mm to (127.0, 63.5)
- moved J11 2.54 mm to (121.9, 53.3)
- moved R2 1.93 mm to (142.2, 76.2)
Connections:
- net /EXT_0 renamed /EXT_8
- net /EXT_1 renamed /EXT_9
- net /EXT_2 renamed /EXT_10
- net /EXT_3 renamed /EXT_11
- net /EXT_4 renamed /EXT_12
- net /EXT_5 renamed /EXT_13
- net /EXT_6 renamed /EXT_14
- net /EXT_7 renamed /EXT_15
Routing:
- net /LED_~{OE}: track 0.00 -> 189.9 mm, vias 0 -> 2
- net VCC: track 337.5 -> 504.8 mm, vias 4 -> 8
- net /ADDRESSED: track 6.13 -> 113.4 mm, vias 0 -> 4
- net /~{RFM}/WTM: track 11.2 -> 117.3 mm, vias 0 -> 7
- net /MEM_ACT: track 6.13 -> 95.6 mm, vias 0 -> 4
- net /CONTENT_12: track 187.8 -> 259.4 mm, vias 2 -> 4
- net /CONTENT_13: track 183.0 -> 246.4 mm, vias 2 -> 4
- net /CONTENT_14: track 183.3 -> 238.7 mm, vias 2 -> 4
- net /CONTENT_15: track 178.5 -> 231.4 mm, vias 2 -> 4
- net Net-(D15-A): track 0.00 -> 26.5 mm
- net Net-(D1-A): track 0.00 -> 26.1 mm
- net Net-(D9-A): track 0.00 -> 25.7 mm
- net Net-(D7-A): track 0.00 -> 25.1 mm
- net Net-(D8-A): track 0.00 -> 23.6 mm
- net Net-(D16-A): track 0.00 -> 23.6 mm
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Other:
- board text added: "0"
- board text added: "1"
- board text added: "10"
- board text added: "11"
- board text added: "12"
- board text added: "13"
- board text added: "14"
- board text added: "15"
- board text added: "2"
- board text added: "3"
- board text added: "4"
- board text added: "5"
- board text added: "6"
- board text added: "7"
- board text added: "8"
- board text added: "9"
- board text added: "ADDRESSED"
- board text added: "CONTENT"
- board text added: "EXT. INPUT"
- board text added: "GND"
- board text added: "JLCJLCJLCJLC"
- board text added: "LED ~{OE}"
- board text added: "Status Word"
- board text added: "VCC"
- board text added: "v. 1.0"

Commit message: Tech check on status word complete
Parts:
- C97, C98, C99: value C_Polarized -> 33uF
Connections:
- U4 pad 1: unconnected-(U4-DIR-Pad1) -> GND
- U5 pad 1: unconnected-(U5-DIR-Pad1) -> GND
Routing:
- net /DATA_BUS_00: track 116.1 -> 112.8 mm
- net /DATA_BUS_01: track 109.2 -> 107.1 mm
- net VCC: track 504.8 -> 506.4 mm
- net /CONTENT_00: track 210.2 -> 209.0 mm
- net /DATA_BUS_08: track 127.6 -> 126.5 mm
- net /DATA_BUS_02: track 102.4 -> 101.5 mm
- net /DATA_BUS_07: track 106.6 -> 105.8 mm
- net /DATA_BUS_06: track 104.2 -> 103.4 mm
- net /CONTENT_07: track 204.0 -> 203.4 mm
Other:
- board text added: "STATUS WORD"
- board text removed: "Status Word"
